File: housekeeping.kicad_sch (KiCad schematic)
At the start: 5 parts, among them U2 TPS7B8133QDGNRQ1

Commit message: Layed on board. Still need to route
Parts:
- removed C17, C18: 10uF, Capacitor_SMD:C_0805_2012Metric, symbol Device:C
- removed TP1: 3V3, _NavLights:HARWIN_S1751-46R, symbol Connector:TestPoint
- removed TP2: TP_GND, _NavLights:HARWIN_S1751-46R, symbol Connector:TestPoint
- removed U2: TPS7B8133QDGNRQ1, _NavLights:VSSOP8_DGN_TEX, symbol _TPS7B81-Q1:TPS7B8133QDGNRQ1
- added C22, C23: 10uF, Capacitor_SMD:C_0805_2012Metric, symbol Device:C
- added U12: TPS7B8133QDGNRQ1, _BMS:VSSOP8_DGN_TEX, symbol _TPS7B:TPS7B8133DRVR
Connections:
- net +3V3: now also C23.1, U12.6 (OUT)
- net 5V_IN: now also C22.1, U12.1 (IN), U12.2 (EN)
- net GND: now also C22.2, C23.2, U12.3 (GND), U12.4 (GND), U12.7 (EXP)
- no-connect marks 0 -> 1

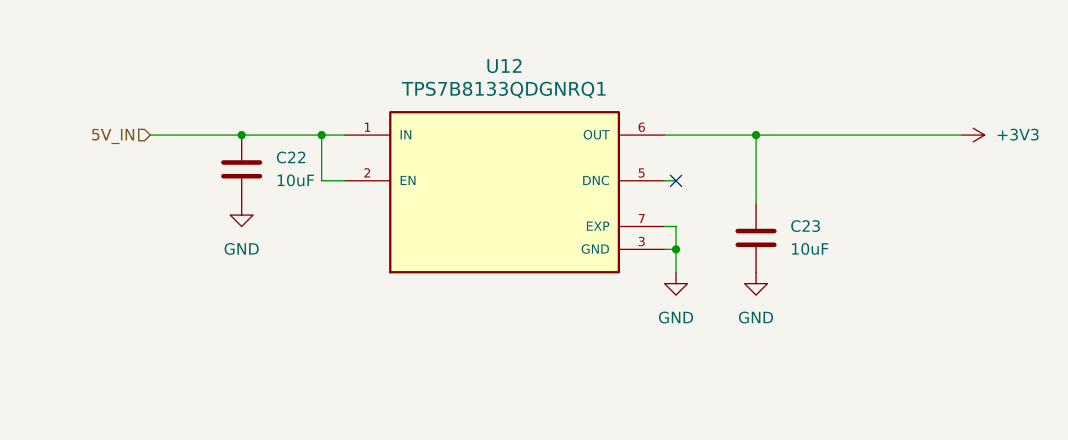
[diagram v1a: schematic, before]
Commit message: Adding proper grounding
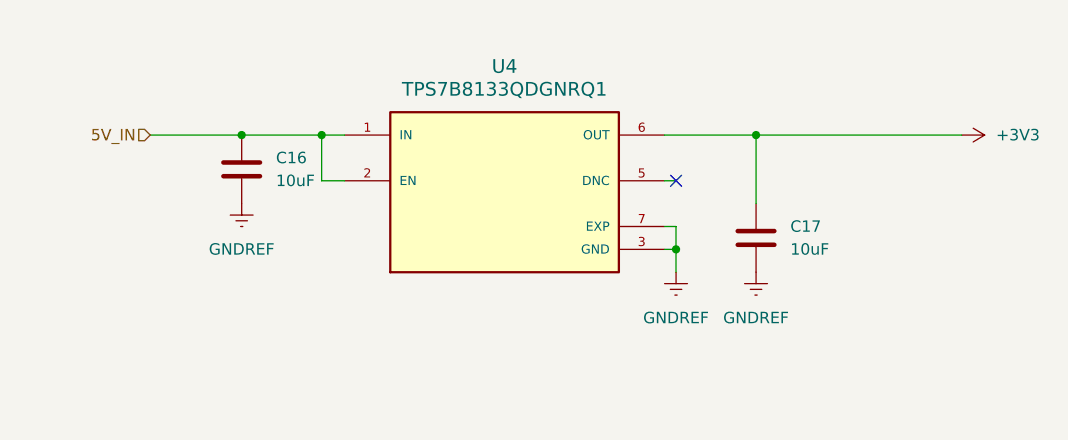
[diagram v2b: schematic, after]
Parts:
- renumbered C22 to C16, C23 to C17, U12 to U4
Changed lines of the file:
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@@
 		(dnp no)
 		(fields_autoplaced yes)
-		(property "Reference" "#PWR065"
+		(property "Reference" "#PWR046"
 			(at 193.04 91.44 0)
 			(effects
@@
 			(project "BMS"
 				(path "/124184ba-5d68-4d9f-8da6-acc6720ab30b/93f9b420-7cce-46a9-9201-666f07a18f85/1875dae8-5675-4324-bc32-eabf0e306a05"
-					(reference "#PWR065")
+					(reference "#PWR046")
 					(unit 1)
 				)
@@
 		(dnp no)
 		(fields_autoplaced yes)
-		(property "Reference" "U12"
+		(property "Reference" "U4"
 			(at 146.05 83.82 0)
 			(effects
@@
 			(project "BMS"
 				(path "/124184ba-5d68-4d9f-8da6-acc6720ab30b/93f9b420-7cce-46a9-9201-666f07a18f85/1875dae8-5675-4324-bc32-eabf0e306a05"
-					(reference "U12")
+					(reference "U4")
 					(unit 1)
 				)
@@
 	)
 	(symbol
-		(lib_id "power:GND")
+		(lib_id "power:GNDREF")
 		(at 116.84 99.06 0)
 		(unit 1)
@@
 		(dnp no)
 		(fields_autoplaced yes)
-		(property "Reference" "#PWR062"
+		(property "Reference" "#PWR043"
 			(at 116.84 105.41 0)
 			(effects
@@
 			)
 		)
-		(property "Value" "GND"
+		(property "Value" "GNDREF"
 			(at 116.84 104.14 0)
 			(effects
@@
 			)
 		)
-		(property "Description" "Power symbol creates a global label with name \"GND\" , ground"
+		(property "Description" "Power symbol creates a global label with name \"GNDREF\" , reference supply ground"
 			(at 116.84 99.06 0)
 			(effects
@@
 			(project "BMS"
 				(path "/124184ba-5d68-4d9f-8da6-acc6720ab30b/93f9b420-7cce-46a9-9201-666f07a18f85/1875dae8-5675-4324-bc32-eabf0e306a05"
-					(reference "#PWR062")
+					(reference "#PWR043")
 					(unit 1)
 				)
@@
 	)
 	(symbol
-		(lib_id "power:GND")
+		(lib_id "power:GNDREF")
+		(at 173.99 106.68 0)
+		(unit 1)
+		(exclude_from_sim no)
+		(in_bom yes)
+		(on_board yes)
+		(dnp no)
+		(fields_autoplaced yes)
+		(property "Reference" "#PWR045"
+			(at 173.99 113.03 0)
+			(effects
+				(font
+					(size 1.27 1.27)
+				)
+				(hide yes)
+			)
+		)
+		(property "Value" "GNDREF"
+			(at 173.99 111.76 0)
+			(effects
+				(font
+					(size 1.27 1.27)
+				)
+			)
+		)
+		(property "Footprint" ""
+			(at 173.99 106.68 0)
+			(effects
+				(font
+					(size 1.27 1.27)
+				)
+				(hide yes)
+			)
+		)
+		(property "Datasheet" ""
+			(at 173.99 106.68 0)
+			(effects
+				(font
+					(size 1.27 1.27)
+				)
+				(hide yes)
+			)
+		)
+		(property "Description" "Power symbol creates a global label with name \"GNDREF\" , reference supply ground"
+			(at 173.99 106.68 0)
+			(effects
+				(font
+					(size 1.27 1.27)
+				)
+				(hide yes)
+			)
+		)
+		(pin "1"
+		)
+		(instances
+			(project "BMS"
+				(path "/124184ba-5d68-4d9f-8da6-acc6720ab30b/93f9b420-7cce-46a9-9201-666f07a18f85/1875dae8-5675-4324-bc32-eabf0e306a05"
+					(reference "#PWR045")
+					(unit 1)
+				)
+			)
+		)
+	)
+	(symbol
+		(lib_id "power:GNDREF")
 		(at 165.1 106.68 0)
 		(unit 1)
@@
 		(dnp no)
 		(fields_autoplaced yes)
-		(property "Reference" "#PWR063"
+		(property "Reference" "#PWR044"
 			(at 165.1 113.03 0)
 			(effects
@@
 			)
 		)
-		(property "Value" "GND"
+		(property "Value" "GNDREF"
 			(at 165.1 111.76 0)
 			(effects
@@
 			)
 		)
-		(property "Description" "Power symbol creates a global label with name \"GND\" , ground"
+		(property "Description" "Power symbol creates a global label with name \"GNDREF\" , reference supply ground"
 			(at 165.1 106.68 0)
 			(effects
@@
 			(project "BMS"
 				(path "/124184ba-5d68-4d9f-8da6-acc6720ab30b/93f9b420-7cce-46a9-9201-666f07a18f85/1875dae8-5675-4324-bc32-eabf0e306a05"
-					(reference "#PWR063")
-					(unit 1)
-				)
-			)
-		)
-	)
-	(symbol
-		(lib_id "power:GND")
-		(at 173.99 106.68 0)
-		(unit 1)
-		(exclude_from_sim no)
-		(in_bom yes)
-		(on_board yes)
-		(dnp no)
-		(fields_autoplaced yes)
-		(property "Reference" "#PWR064"
-			(at 173.99 113.03 0)
-			(effects
-				(font
-					(size 1.27 1.27)
-				)
-				(hide yes)
-			)
-		)
-		(property "Value" "GND"
-			(at 173.99 111.76 0)
-			(effects
-				(font
-					(size 1.27 1.27)
-				)
-			)
-		)
-		(property "Footprint" ""
-			(at 173.99 106.68 0)
-			(effects
-				(font
-					(size 1.27 1.27)
-				)
-				(hide yes)
-			)
-		)
-		(property "Datasheet" ""
-			(at 173.99 106.68 0)
-			(effects
-				(font
-					(size 1.27 1.27)
-				)
-				(hide yes)
-			)
-		)
-		(property "Description" "Power symbol creates a global label with name \"GND\" , ground"
-			(at 173.99 106.68 0)
-			(effects
-				(font
-					(size 1.27 1.27)
-				)
-				(hide yes)
-			)
-		)
-		(pin "1"
-		)
-		(instances
-			(project "BMS"
-				(path "/124184ba-5d68-4d9f-8da6-acc6720ab30b/93f9b420-7cce-46a9-9201-666f07a18f85/1875dae8-5675-4324-bc32-eabf0e306a05"
-					(reference "#PWR064")
+					(reference "#PWR044")
 					(unit 1)
 				)
@@
 		(dnp no)
 		(fields_autoplaced yes)
-		(property "Reference" "C22"
+		(property "Reference" "C16"
 			(at 120.65 93.9799 0)
 			(effects
@@
 			(project "BMS"
 				(path "/124184ba-5d68-4d9f-8da6-acc6720ab30b/93f9b420-7cce-46a9-9201-666f07a18f85/1875dae8-5675-4324-bc32-eabf0e306a05"
-					(reference "C22")
+					(reference "C16")
 					(unit 1)
 				)
@@
 		(dnp no)
 		(fields_autoplaced yes)
-		(property "Reference" "C23"
+		(property "Reference" "C17"
 			(at 177.8 101.5999 0)
 			(effects
@@
 			(project "BMS"
 				(path "/124184ba-5d68-4d9f-8da6-acc6720ab30b/93f9b420-7cce-46a9-9201-666f07a18f85/1875dae8-5675-4324-bc32-eabf0e306a05"
-					(reference "C23")
+					(reference "C17")
 					(unit 1)
 				)

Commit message: Lots of changfes
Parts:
- renumbered C16 to C17, C17 to C18
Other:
- moved on the sheet: C17

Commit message: Updating stuff
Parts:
- removed U4: TPS7B8133QDGNRQ1, _BMS:VSSOP8_DGN_TEX, symbol _TPS7B:TPS7B8133DRVR
- added U4: TPS7B8133QDGNRQ1, VSSOP8_DGN_TEX, symbol _TPS7B:TPS7B8133QDGNRQ1
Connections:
- net +3V3: now also U4.8 (OUT)
- net 5V_IN: now also U4.1 (IN), U4.2 (EN)
- net GND: now also U4.4 (GND), U4.5 (GND), U4.6 (GND), U4.9 (EPAD)
- no-connect marks 1 -> 0
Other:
- moved on the sheet: C17, C18

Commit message: Placement
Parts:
- U4: footprint VSSOP8_DGN_TEX -> _BMS:VSSOP8_DGN_TEX
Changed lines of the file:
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@@
 		(dnp no)
 		(fields_autoplaced yes)
-		(property "Reference" "#PWR072"
+		(property "Reference" "#PWR048"
 			(at 175.26 99.06 0)
 			(effects
@@
 			(project "BMS"
 				(path "/124184ba-5d68-4d9f-8da6-acc6720ab30b/93f9b420-7cce-46a9-9201-666f07a18f85/1875dae8-5675-4324-bc32-eabf0e306a05"
-					(reference "#PWR072")
+					(reference "#PWR048")
 					(unit 1)
 				)
@@
 		(dnp no)
 		(fields_autoplaced yes)
-		(property "Reference" "#PWR048"
+		(property "Reference" "#PWR046"
 			(at 115.57 120.65 0)
 			(effects
@@
 			(project ""
 				(path "/124184ba-5d68-4d9f-8da6-acc6720ab30b/93f9b420-7cce-46a9-9201-666f07a18f85/1875dae8-5675-4324-bc32-eabf0e306a05"
-					(reference "#PWR048")
+					(reference "#PWR046")
 					(unit 1)
 				)
@@
 			)
 		)
-		(property "Footprint" "VSSOP8_DGN_TEX"
+		(property "Footprint" "_BMS:VSSOP8_DGN_TEX"
 			(at 127 99.06 0)
 			(effects
@@
 		(dnp no)
 		(fields_autoplaced yes)
-		(property "Reference" "#PWR071"
+		(property "Reference" "#PWR047"
 			(at 125.73 120.65 0)
 			(effects
@@
 			(project "BMS"
 				(path "/124184ba-5d68-4d9f-8da6-acc6720ab30b/93f9b420-7cce-46a9-9201-666f07a18f85/1875dae8-5675-4324-bc32-eabf0e306a05"
-					(reference "#PWR071")
+					(reference "#PWR047")
 					(unit 1)
 				)

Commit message: Working on routing
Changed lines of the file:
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@@
+	)
+	(symbol
+		(lib_id "power:PWR_FLAG")
+		(at 115.57 99.06 0)
+		(unit 1)
+		(exclude_from_sim no)
+		(in_bom yes)
+		(on_board yes)
+		(dnp no)
+		(fields_autoplaced yes)
+		(property "Reference" "#FLG08"
+			(at 115.57 97.155 0)
+			(effects
+				(font
+					(size 1.27 1.27)
+				)
+				(hide yes)
+			)
+		)
+		(property "Value" "PWR_FLAG"
+			(at 115.57 93.98 0)
+			(effects
+				(font
+					(size 1.27 1.27)
+				)
+			)
+		)
+		(property "Footprint" ""
+			(at 115.57 99.06 0)
+			(effects
+				(font
+					(size 1.27 1.27)
+				)
+				(hide yes)
+			)
+		)
+		(property "Datasheet" "~"
+			(at 115.57 99.06 0)
+			(effects
+				(font
+					(size 1.27 1.27)
+				)
+				(hide yes)
+			)
+		)
+		(property "Description" "Special symbol for telling ERC where power comes from"
+			(at 115.57 99.06 0)
+			(effects
+				(font
+					(size 1.27 1.27)
+				)
+				(hide yes)
+			)
+		)
+		(pin "1"
+		)
+		(instances
+			(project ""
+				(path "/124184ba-5d68-4d9f-8da6-acc6720ab30b/93f9b420-7cce-46a9-9201-666f07a18f85/1875dae8-5675-4324-bc32-eabf0e306a05"
+					(reference "#FLG08")
+					(unit 1)
+				)
+			)
+		)
 	)
 	(symbol

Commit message: Pushing
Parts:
- added D23: LED, symbol Device:LED
- added R36: R, symbol Device:R
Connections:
- net +3V3: now also R36.1
- net GND: now also D23.1 (K)
- new net: D23.2 (A), R36.2
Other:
- moved on the sheet: C17, C18
